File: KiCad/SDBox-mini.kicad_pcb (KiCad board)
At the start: 2 copper layers, 36.7 x 34 mm, 24 parts, among them J1 DB25_Male, J2 Conn_01x06, J3 Micro_SD_Card, J4 USB_B_Micro, U1 ATmega328P-AU, U2 LM1117-3.3, U3 74LVC3G17, U4 74HCT2G17, Y1 Crystal_GND24_Small

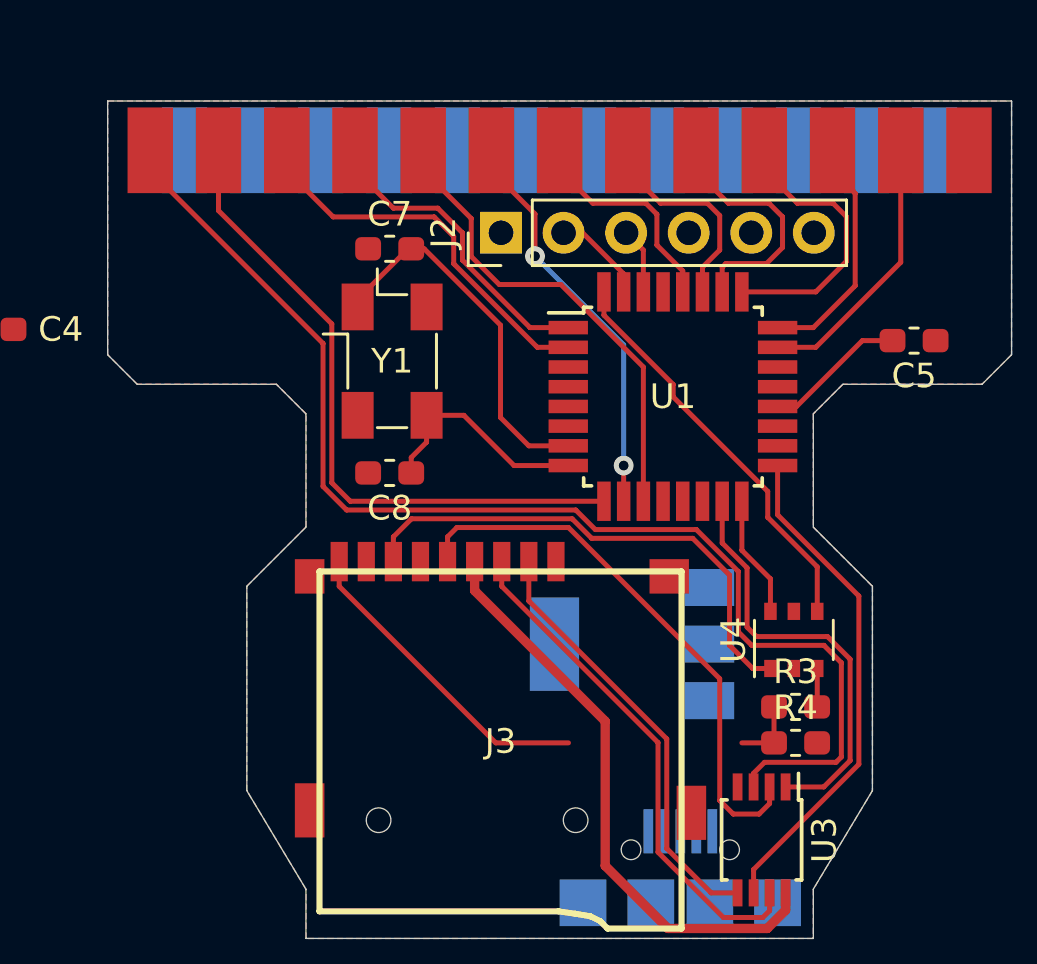
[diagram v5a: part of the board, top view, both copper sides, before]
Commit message: adapted for new pinout and rerouted
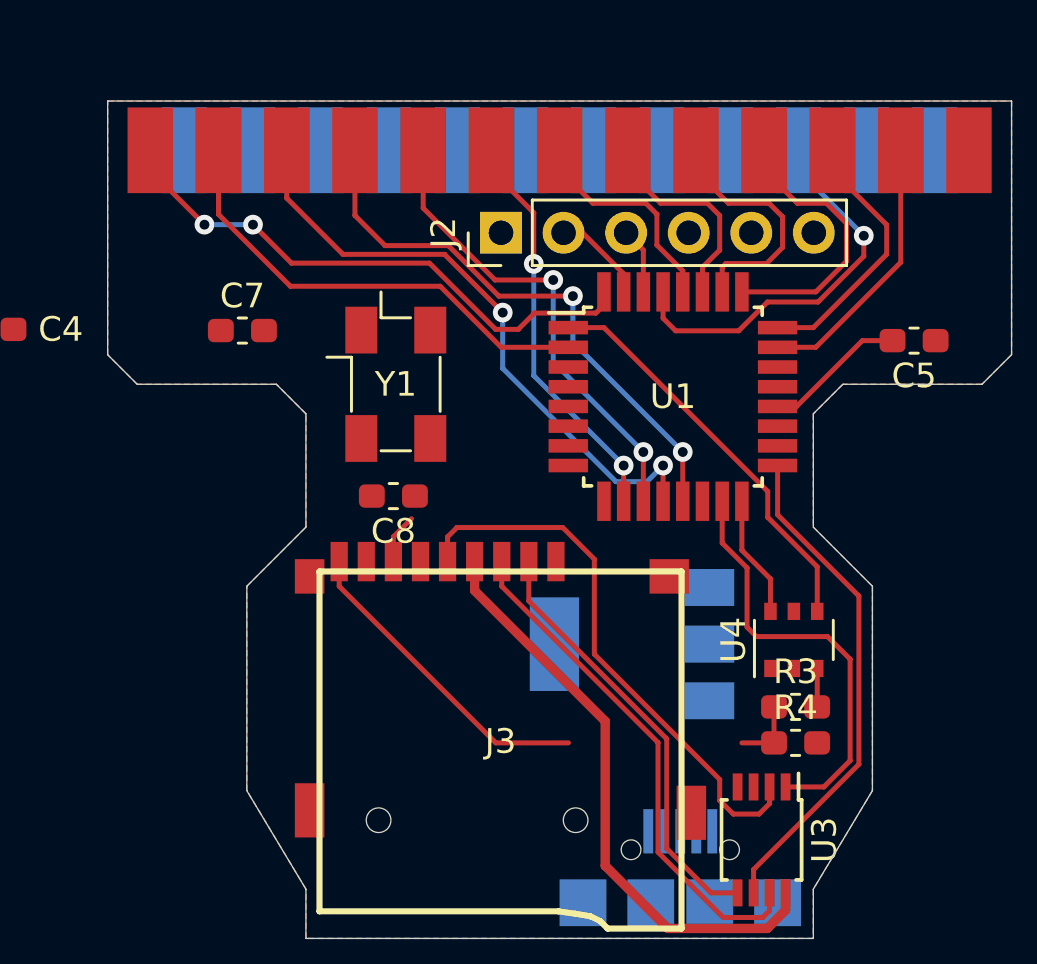
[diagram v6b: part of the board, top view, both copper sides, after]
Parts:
- moved C7 6.84 mm to (93.6, 59.3)
- moved C8 0.95 mm to (99.8, 66.0)
- moved Y1 0.95 mm to (99.8, 61.5)
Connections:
- J1 pad 1: (no net) -> Net-(J1-Pad1)
- J1 pad 14: (no net) -> Net-(J1-Pad14)
- J1 pad 15: (no net) -> Net-(J1-Pad15)
- J1 pad 23: (no net) -> Net-(J1-Pad23)
- J1 pad 24: (no net) -> Net-(J1-Pad24)
- J1 pad 25: (no net) -> Net-(J1-Pad25)
- J3 pad 1: (no net) -> Net-(J3-Pad1)
- J3 pad 8: (no net) -> Net-(J3-Pad8)
- J3 pad 9: CARD_DETECT -> CD
- J4 pad 2: (no net) -> Net-(J4-Pad2)
- J4 pad 3: (no net) -> Net-(J4-Pad3)
- J4 pad 4: (no net) -> Net-(J4-Pad4)
- R3 pad 1: CARD_DETECT -> CD
- R4 pad 1: CARD_DETECT -> CD
- U1 pad 1: ACK -> CP
- U1 pad 12: (no net) -> BUSY
- U1 pad 13: (no net) -> ACK
- U1 pad 14: (no net) -> SS
- U1 pad 19: (no net) -> Net-(U1-Pad19)
- U1 pad 2: BUSY -> POUT
- U1 pad 22: (no net) -> Net-(U1-Pad22)
- U1 pad 32: CD -> SELECT
- U1 pad 9: POUT -> Net-(U1-Pad9)
- U3 pad 3: SELECT -> SS
- U4 pad 4: CD -> CP
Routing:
- net SELECT: track 50.2 -> 22.9 mm, vias 0 -> 2
- net MISO_3V3: track 20.8 -> 2.04 mm
- net CP: track 0.00 -> 16.6 mm
- net RESET: track 0.00 -> 16.1 mm, vias 0 -> 1
- net CARD_DETECT: track 15.7 -> 0.00 mm
- net /XTAL1: track 15.2 -> 0.00 mm
- net ACK: track 12.8 -> 23.3 mm, vias 0 -> 2
- net /XTAL2: track 9.19 -> 0.00 mm
- net BUSY: track 15.9 -> 25.0 mm, vias 0 -> 2
- net POUT: track 26.8 -> 19.0 mm
- net D1: track 9.74 -> 10.8 mm
- net CD: track 16.6 -> 15.7 mm
- net D7: track 19.4 -> 19.3 mm, vias 0 -> 2

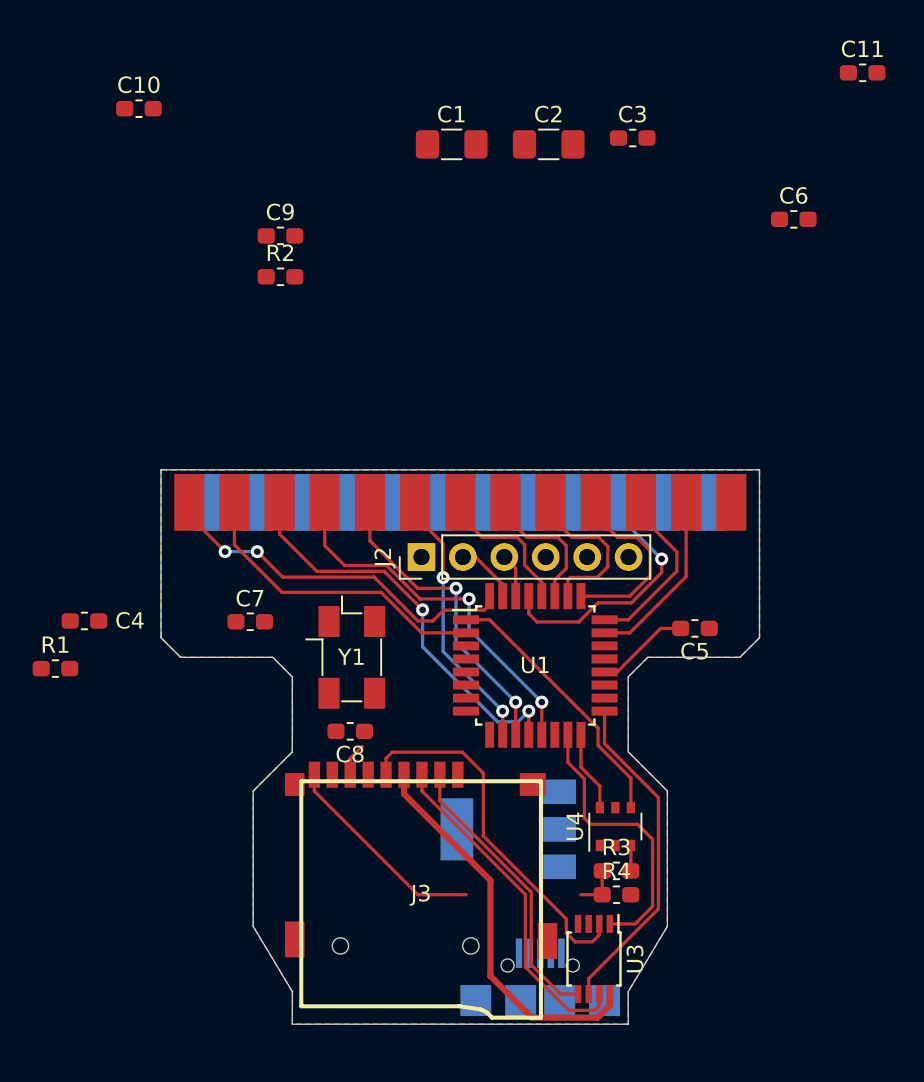
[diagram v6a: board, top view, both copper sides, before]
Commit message: imporved routing and small fix of micro-usb footprint
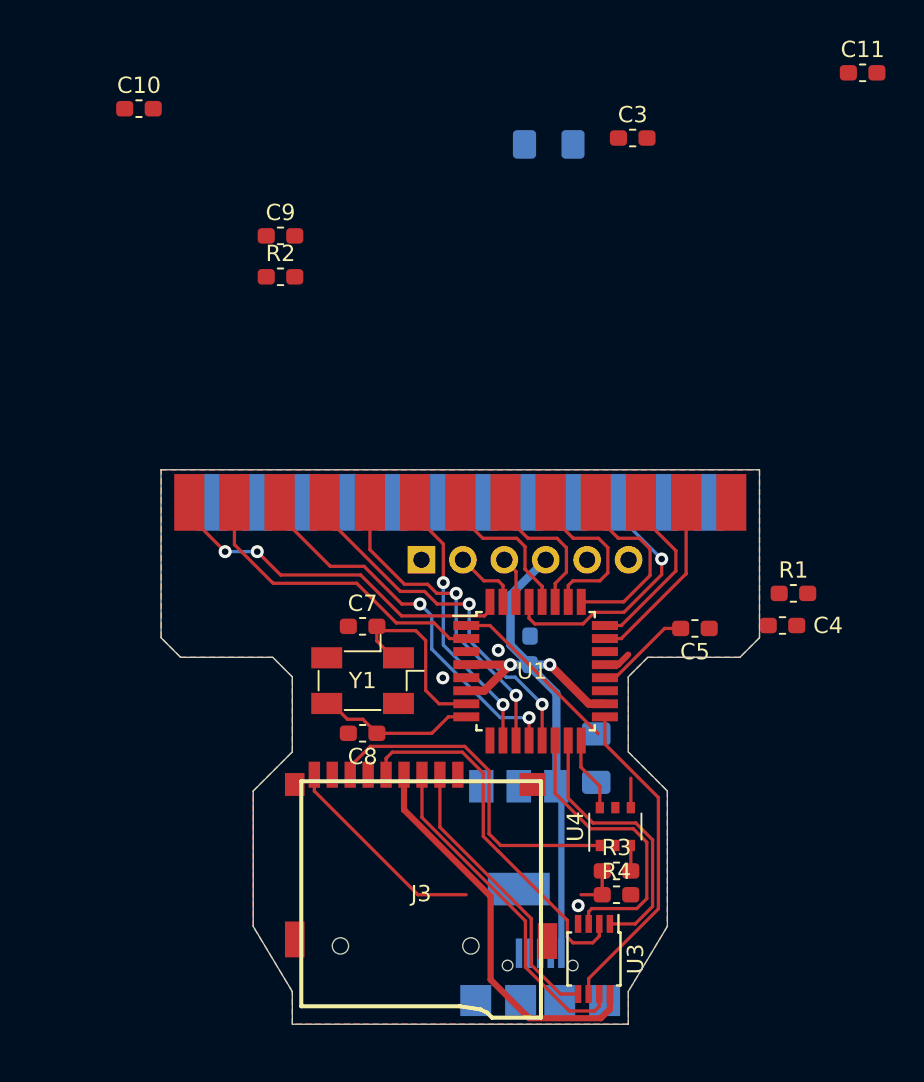
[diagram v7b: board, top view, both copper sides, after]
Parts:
- C1, C2, C6: moved to B.Cu
- moved R1 45.5 mm to (126.9, 57.6)
- moved C4 42.8 mm to (126.3, 59.5)
- moved C1 38.7 mm to (114.8, 67.7), turned to 90 degrees
- moved C6 31.0 mm to (110.8, 61.1), turned to 270 degrees
- moved C7 6.90 mm to (100.5, 59.6)
- moved Y1 1.57 mm to (100.5, 62.9), turned to 180 degrees
- moved U2 0.83 mm to (110.1, 72.6), turned to 270 degrees
- moved C8 0.77 mm to (100.5, 66.2)
- moved U1 0.35 mm to (111.1, 62.4)
- moved J2 0.17 mm to (104.1, 55.5)
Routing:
- net VCC: track 0.00 -> 39.2 mm, vias 0 -> 2
- net MISO_3V3: track 2.04 -> 21.1 mm
- net SS: track 0.00 -> 18.2 mm
- net /XTAL1: track 0.00 -> 11.9 mm
- net /XTAL2: track 0.00 -> 9.74 mm
- net CP: track 16.6 -> 12.6 mm
- net GND: track 0.00 -> 1.69 mm, vias 0 -> 3
- net BUSY: track 25.0 -> 23.8 mm
- net ACK: track 23.3 -> 22.5 mm
- net MOSI: track 17.4 -> 16.9 mm
- net D7: track 19.3 -> 19.8 mm

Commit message: reshaped PCB outline to accomodate LED indicators
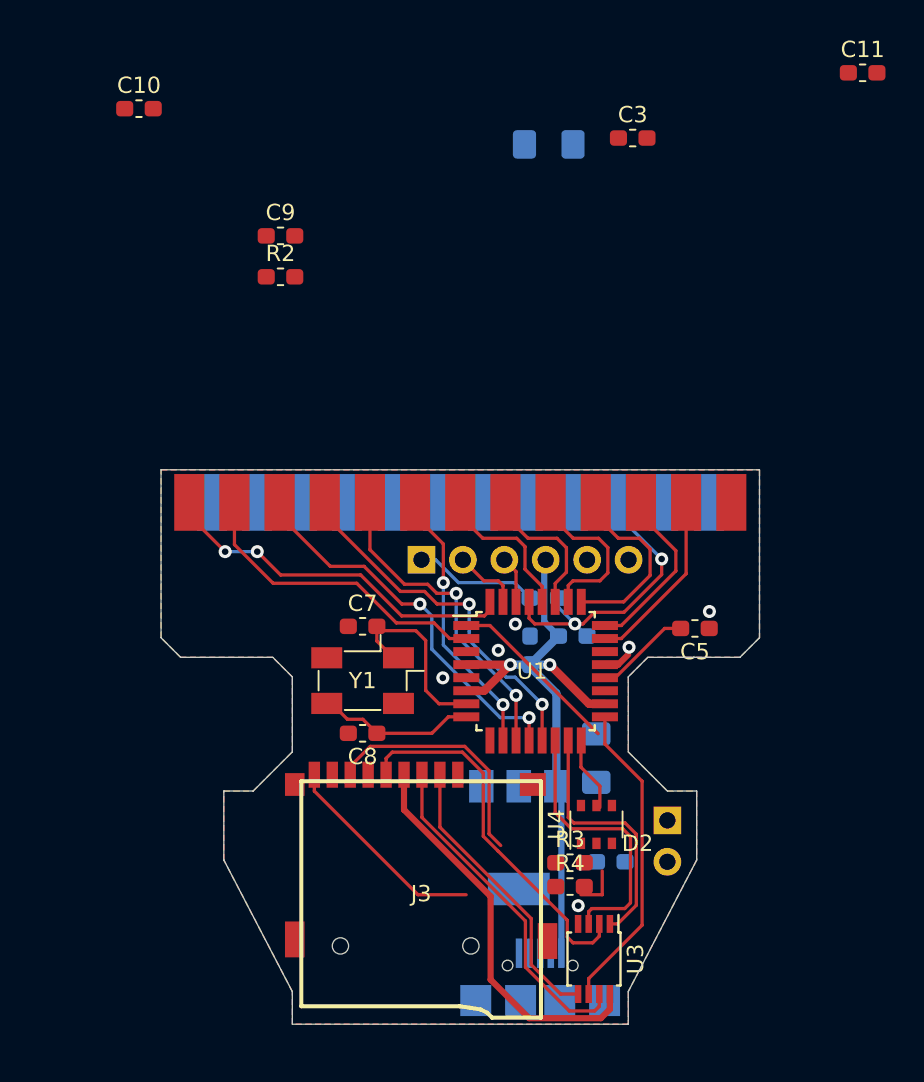
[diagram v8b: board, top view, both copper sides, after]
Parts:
- added D2: LED, Connector_PinHeader_2.54mm:PinHeader_1x02_P2.54mm_Vertical, F.Cu at (119.2, 71.5)
- added R5: 150, Resistor_SMD:R_0603_1608Metric_Pad1.05x0.95mm_HandSolder, B.Cu at (115.7, 74.0)
- C4, R1: moved to B.Cu
- moved C4 14.7 mm to (111.7, 57.9), turned to 180 degrees
- moved R1 13.8 mm to (113.4, 60.2), turned to 180 degrees
- moved R3 2.89 mm to (113.2, 74.1)
- moved R4 2.89 mm to (113.2, 75.6)
- moved U4 1.17 mm to (114.8, 71.8)
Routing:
- net DTR: track 0.00 -> 7.63 mm
- net MISO_3V3: track 21.1 -> 15.0 mm
- net RESET: track 16.1 -> 19.1 mm, vias 1 -> 2
- net CP: track 12.6 -> 10.8 mm
- net Net-(C11-Pad1): track 1.56 -> 0.00 mm
- net MOSI: track 16.9 -> 15.8 mm
- net SS: track 18.2 -> 17.3 mm
- net SCK: track 20.1 -> 19.3 mm
- net GND: vias 3 -> 6
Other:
- outline, holes or cut-outs redrawn
